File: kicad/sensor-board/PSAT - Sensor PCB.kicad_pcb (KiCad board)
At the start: 2 copper layers, 54.5 x 54.5 mm, 36 parts, among them J1 Conn_01x06, J2 Conn_01x02, J3 Conn_01x03_Pin, J4 Conn_01x03, J6 MCU - Conn_01x04, Q1 Q_NPN_BCE, U1 MPU-6000, U2 BME280, U3 ADXL375, U4 CD-PA1616D, U5 ESP32-CAM

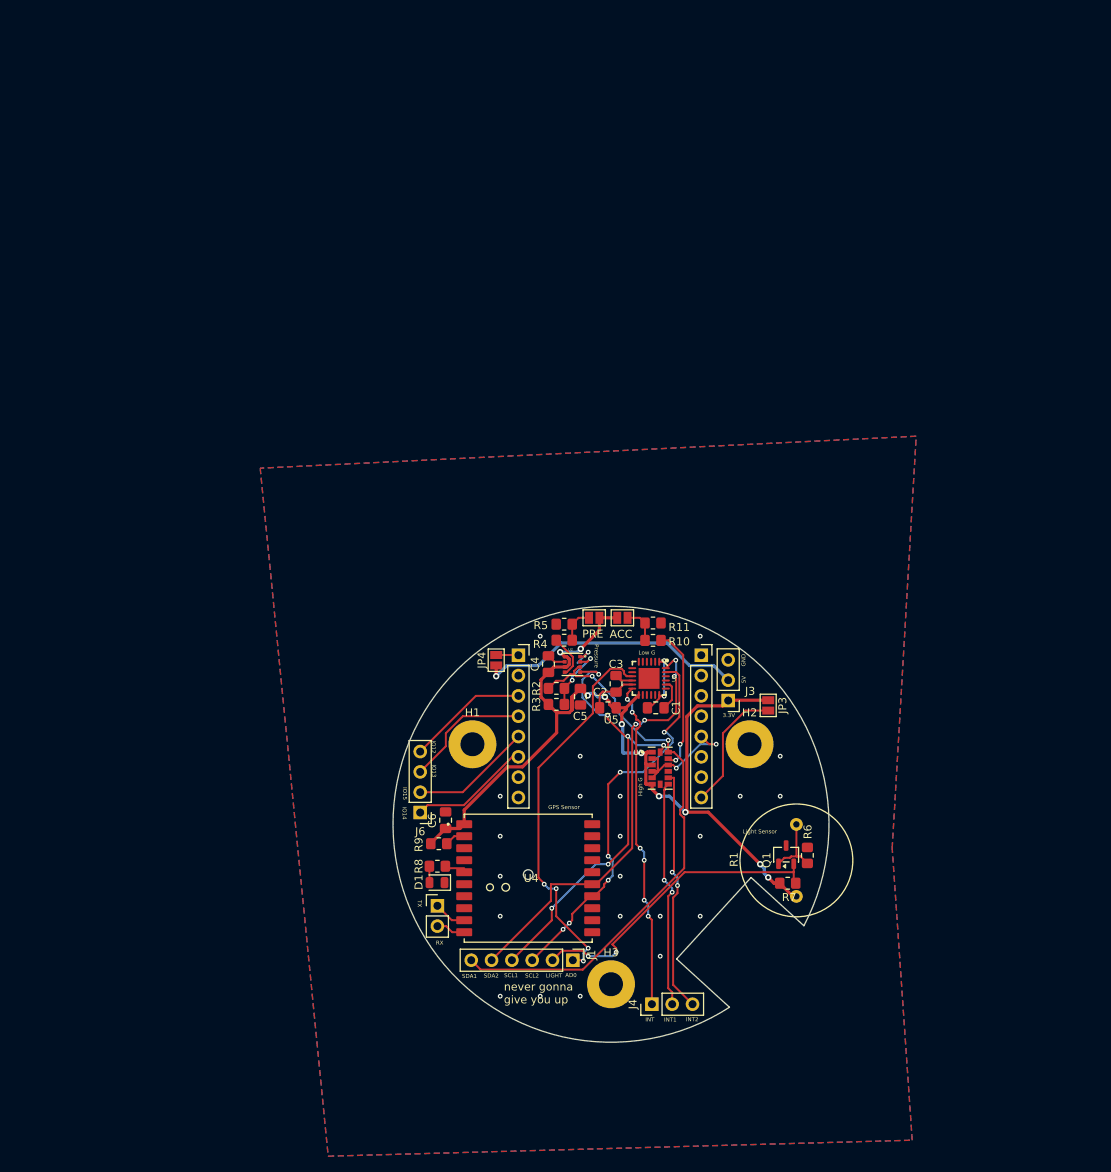
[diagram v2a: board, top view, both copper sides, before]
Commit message: feat: new sensor board pcb & schematic (after feedback)
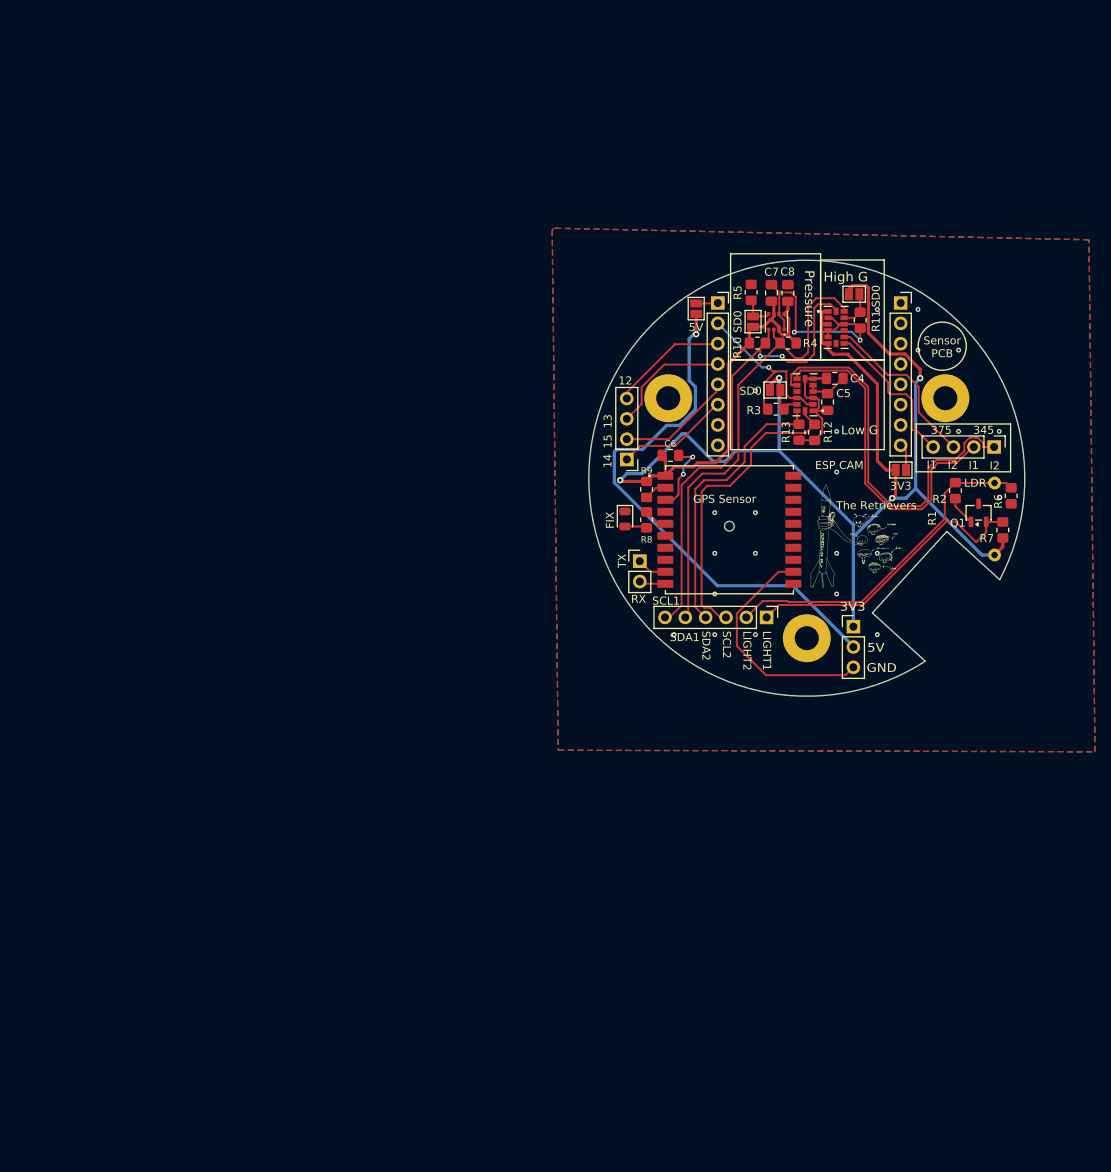
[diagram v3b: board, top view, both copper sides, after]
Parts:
- removed C1: 2.2n, Capacitor_SMD:C_0805_2012Metric_Pad1.18x1.45mm_HandSolder
- removed C2: 0.1n, Capacitor_SMD:C_0805_2012Metric_Pad1.18x1.45mm_HandSolder
- removed C3: 0.1μ, Capacitor_SMD:C_0805_2012Metric_Pad1.18x1.45mm_HandSolder
- removed J4: Conn_01x03, Connector_PinHeader_2.54mm:PinHeader_1x03_P2.54mm_Vertical
- removed JP1, JP2, JP3, JP4: EN_5, Jumper:SolderJumper-2_P1.3mm_Open_Pad1.0x1.5mm
- removed U1: MPU-6000, mpu6000:QFN-24-EP
- added 3V3: EN_5, Jumper:SolderJumper-2_P1.3mm_Open_Pad1.0x1.5mm, F.Cu at (154.1, 96.2)
- added 5V: EN_5, Jumper:SolderJumper-2_P1.3mm_Open_Pad1.0x1.5mm, F.Cu at (128.5, 76.0)
- added C7: 100nF, Capacitor_SMD:C_0805_2012Metric_Pad1.18x1.45mm_HandSolder, F.Cu at (137.9, 74.1)
- added C8: 100nF, Capacitor_SMD:C_0805_2012Metric_Pad1.18x1.45mm_HandSolder, F.Cu at (140.0, 74.1)
- added G***: LOGO, LOGO, F.Cu at (148.5, 105.8)
- added G***: LOGO, LOGO, B.Cu at (142.1, 84.1)
- added J7: Conn_01x06, Connector_PinHeader_2.54mm:PinHeader_1x06_P2.54mm_Vertical, F.Cu at (137.3, 114.7)
- added R12: 4.7k, Resistor_SMD:R_0805_2012Metric_Pad1.20x1.40mm_HandSolder, F.Cu at (143.3, 91.5)
- added R13: 4.7k, Resistor_SMD:R_0805_2012Metric_Pad1.20x1.40mm_HandSolder, F.Cu at (141.3, 91.5)
- added SD0: EN_5, Jumper:SolderJumper-2_P1.3mm_Open_Pad1.0x1.5mm, F.Cu at (138.4, 86.2)
- added SD0: EN_5, Jumper:SolderJumper-2_P1.3mm_Open_Pad1.0x1.5mm, F.Cu at (135.6, 77.7)
- added SD0: EN_5, Jumper:SolderJumper-2_P1.3mm_Open_Pad1.0x1.5mm, F.Cu at (148.2, 74.2)
- added U6: BME280, bme280:PSON65P250X250X100-8N, F.Cu at (138.5, 77.7)
- C4, C5: value 100n -> 100nF
- J1: value Conn_01x06 -> Conn_01x04; footprint Connector_PinHeader_2.54mm:PinHeader_1x06_P2.54mm_Vertical -> Connector_PinHeader_2.54mm:PinHeader_1x04_P2.54mm_Vertical
- Q1: value Q_NPN_BCE -> 2N2222A
- R1: footprint OptoDevice:R_LDR_D13.8mm_P9.0mm_Vertical -> PSAT_Library:ldr
- R10, R4: value 1k5 -> 4.7k
- R2: value 4.7k -> 100k
- R3: value 4.7k -> 1Meg
- R9: value 180k -> 10k
- U2: value BME280 -> ADXL345; footprint bme280:PSON65P250X250X100-8N -> ADXL345:adxl345
- U3: footprint ADXL375:PQFN80P500X300X100-14N -> ADXL375:adxl375
- moved J1 83.0 mm to (165.7, 93.3)
- moved U3 59.3 mm to (146.0, 78.4)
- moved R2 55.7 mm to (160.9, 98.8), turned to -90 degrees
- moved C6 53.6 mm to (125.3, 94.4), turned to 0 degrees
- moved R7 51.7 mm to (166.8, 103.7), turned to -90 degrees
- moved R6 51.7 mm to (167.9, 99.5), turned to 90 degrees
- moved R9 51.3 mm to (122.3, 98.7), turned to -90 degrees
- moved D1 51.2 mm to (119.6, 102.3), turned to -90 degrees
- moved J6 51.1 mm to (119.8, 94.9)
- moved U5 50.6 mm to (142.8, 83.9)
- moved R8 50.6 mm to (122.3, 102.5), turned to -90 degrees
- moved C4 50.6 mm to (145.8, 84.8), turned to 0 degrees
- moved U4 50.3 mm to (132.7, 103.7)
- moved J2 50.0 mm to (121.5, 107.6)
- moved H1 49.7 mm to (125.0, 87.3)
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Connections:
- net /GPS Reset renamed Net-(U4-~{RESET})
- C4 pad 1: 3.3V -> Net-(U2-RESERVED_3)
- C5 pad 1: 3.3V -> Net-(U2-RESERVED_3)
- J1 pad 1: ADO -> INT2_345
- J1 pad 2: LIGHT -> INT1_345
- J1 pad 3: SCL2 -> INT2_375
- J1 pad 4: SCL1 -> INT1_375
- Q1 pad 2: LIGHT -> LIGHT1
- R1 pad 2: Net-(Q1-B) -> LIGHT2
- R10 pad 1: SDO_ACC -> SCL1
- R10 pad 2: Net-(JP2-B) -> 3.3V
- R11 pad 1: Net-(JP2-B) -> GND
- R11 pad 2: GND -> SDO_ACC1
- R2 pad 1: SDA1 -> LIGHT2
- R2 pad 2: Net-(U2-CSB) -> Net-(Q1-B)
- R3 pad 1: 3.3V -> SDO_ACC2
- R3 pad 2: Net-(U2-CSB) -> GND
- R4 pad 1: SDO_PRESSURE -> SDA1
- R4 pad 2: Net-(JP1-B) -> 3.3V
- R5 pad 1: Net-(JP1-B) -> SDO_PRESSURE
- R6 pad 2: Net-(Q1-B) -> LIGHT2
- R7 pad 1: LIGHT -> LIGHT1
- U2 pad 1: GND -> Net-(U2-RESERVED_3)
- U2 pad 2: Net-(U2-CSB) -> GND
- U2 pad 3: SDA1 -> Net-(U2-RESERVED_3)
- U2 pad 4: SCL1 -> GND
- U2 pad 5: SDO_PRESSURE -> GND
- U2 pad 6: 3.3V -> Net-(U2-RESERVED_3)
- U2 pad 7: GND -> Net-(U2-RESERVED_3)
- U2 pad 8: 3.3V -> INT1_345
- U3 pad 12: SDO_ACC -> SDO_ACC1
- U3 pad 8: Net-(J4-Pin_2) -> INT1_375
- U3 pad 9: Net-(J4-Pin_3) -> INT2_375
- U4 pad 14: SCL2 -> unconnected-(U4-RX1/I2C_SCL-Pad14)
- U4 pad 15: SDA2 -> unconnected-(U4-TX1/I2C_SDA-Pad15)
- U5 pad 13: GND -> unconnected-(U5-GND.-Pad13)
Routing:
- net 3.3V: track 125.3 -> 200.8 mm, vias 10 -> 4
- net GND: track 36.6 -> 98.8 mm
- net INT2_345: track 0.00 -> 49.1 mm
- net ADO: track 48.3 -> 0.00 mm, vias 4 -> 0
- net INT1_345: track 0.00 -> 42.5 mm
- net LIGHT2: track 0.00 -> 42.4 mm
- net INT: track 41.6 -> 0.00 mm, vias 6 -> 0
- net LIGHT: track 39.1 -> 0.00 mm, vias 2 -> 0
- net LIGHT1: track 0.00 -> 37.4 mm
- net 5V: track 34.0 -> 67.4 mm
- net Net-(J4-Pin_3): track 30.6 -> 0.00 mm, vias 2 -> 0
- net Net-(J4-Pin_2): track 28.6 -> 0.00 mm, vias 2 -> 0
- net INT2_375: track 0.00 -> 21.2 mm
- net Net-(U2-RESERVED_3): track 0.00 -> 19.8 mm
- net INT1_375: track 0.00 -> 19.4 mm
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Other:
- board text added: "12"
- board text added: "13"
- board text added: "14"
- board text added: "15"
- board text added: "345"
- board text added: "375"
- board text added: "3V3"
- board text added: "ESP CAM"
- board text added: "FIX"
- board text added: "I1"
- board text added: "I2"
- board text added: "LDR"
- board text added: "LIGHT1"
- board text added: "LIGHT2"
- board text added: "Never gonna give you up Never gonna let you down Never gonna run around and desert you Never gonna make you cry Never gonna say goodbye Never gonna tell a lie and hurt you"
- board text added: "Sensor PCB"
- board text added: "The Retrievers"
- board text removed: "3.3V"
- board text removed: "ACC"
- board text removed: "AD0"
- board text removed: "Dear PSAT Team, We couldnt figure out soldermask expansion errors pls help :)"
- board text removed: "INT"
- board text removed: "INT1"
- board text removed: "INT2"
- board text removed: "IO12"
- board text removed: "IO13"
- board text removed: "IO14"
- board text removed: "IO15"
- board text removed: "LIGHT"
- board text removed: "Light Sensor"
- board text removed: "PRE"
- board text removed: "never gonna give you up"

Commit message: feat: Changed labels & started pcb wiring
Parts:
- removed the J1 at (165.7, 93.3)
- removed J7: Conn_01x06, Connector_PinHeader_2.54mm:PinHeader_1x06_P2.54mm_Vertical
- added J4: 5015680407, footprints:CONN_5015680000-SD_04_MOL, F.Cu at (153.7, 104.7)
- added TP1: TestPoint, TestPoint:TestPoint_Pad_D1.0mm, F.Cu at (97.5, 111.0)
- added TP10: TestPoint, TestPoint:TestPoint_Pad_D1.0mm, F.Cu at (101.5, 111.0)
- added TP11: TestPoint, TestPoint:TestPoint_Pad_D1.0mm, F.Cu at (93.4, 111.0)
- added TP12: TestPoint, TestPoint:TestPoint_Pad_D1.0mm, F.Cu at (93.4, 115.0)
- added TP13: TestPoint, TestPoint:TestPoint_Pad_D1.0mm, F.Cu at (97.5, 94.8)
- added TP14: TestPoint, TestPoint:TestPoint_Pad_D1.0mm, F.Cu at (97.5, 98.8)
- added TP2: TestPoint, TestPoint:TestPoint_Pad_D1.0mm, F.Cu at (97.5, 115.0)
- added TP3: TestPoint, TestPoint:TestPoint_Pad_D1.0mm, F.Cu at (93.4, 94.8)
- added TP4: TestPoint, TestPoint:TestPoint_Pad_D1.0mm, F.Cu at (93.4, 98.8)
- added TP5: TestPoint, TestPoint:TestPoint_Pad_D1.0mm, F.Cu at (93.4, 102.9)
- added TP6: TestPoint, TestPoint:TestPoint_Pad_D1.0mm, F.Cu at (93.4, 107.0)
- added TP7: TestPoint, TestPoint:TestPoint_Pad_D1.0mm, F.Cu at (97.5, 102.9)
- added TP8: TestPoint, TestPoint:TestPoint_Pad_D1.0mm, F.Cu at (97.5, 107.0)
- added TP9: TestPoint, TestPoint:TestPoint_Pad_D1.0mm, F.Cu at (101.5, 107.0)
- C5: renamed from C4; value 100nF -> 1uF
- C7: renamed from C5; value 100nF -> 0.1uF
- J2: value Conn_01x02 -> 5015680407; footprint Connector_PinHeader_2.54mm:PinHeader_1x02_P2.54mm_Vertical -> footprints:CONN_5015680000-SD_04_MOL
- J3: value Conn_01x03_Pin -> 5015680407 (X3); footprint Connector_PinHeader_2.54mm:PinHeader_1x03_P2.54mm_Vertical -> footprints:CONN_5015680000-SD_04_MOL
- moved J2 14.5 mm to (132.5, 117.0), turned to 135 degrees
- moved J3 5.32 mm to (148.5, 110.5), turned to 46.5 degrees
- renumbered C8 to C3, C7 to C4, J6 to J1, 5V to JP1, SD0 to JP2, 3V3 to JP3, SD0 to JP4, SD0 to JP5, R11 to R1, R3 to R10, R9 to R11, R4 to R2, R10 to R3, R6 to R4, R1 to R5, R2 to R6, R5 to R7, R7 to R8, R8 to R9, U5 to U1, U6 to U2, U2 to U4, U4 to U5
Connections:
- net SDO_ACC1 renamed HIGH_G_ADDR
- net SDO_ACC2 renamed LOW_G_ADDR
- net SDO_PRESSURE renamed PRESSURE_ADDR
- C3 pad 2: 3.3V -> 3V3_f
- C4 pad 1: 3.3V -> 3V3_f
- C5 pad 1: Net-(U2-RESERVED_3) -> 3V3_f
- C6 pad 1: 3.3V -> 3V3_uf
- C7 pad 1: Net-(U2-RESERVED_3) -> 3V3_f
- J2 pad 1: GPS_UART_TX -> LIGHT2
- J2 pad 2: GPS_UART_RX -> LIGHT1
- J3 pad 1: 3.3V -> GPS_UART_RX
- J3 pad 2: 5V -> GPS_UART_TX
- J3 pad 3: GND -> SDA1
- JP2 pad 1: 3.3V -> 3V3_f
- JP3 pad 1: 3.3V -> 3V3_f
- JP4 pad 1: 3.3V -> 3V3_f
- JP5 pad 1: 3.3V -> 3V3_f
- R11 pad 1: 3.3V -> 3V3_uf
- R12 pad 1: Net-(U2-RESERVED_3) -> 3V3_f
- R13 pad 1: Net-(U2-RESERVED_3) -> 3V3_f
- R2 pad 2: 3.3V -> 3V3_f
- R3 pad 2: 3.3V -> 3V3_f
- R5 pad 1: 3.3V -> 3V3_f
- R8 pad 2: 3.3V -> 3V3_f
- R9 pad 1: Net-(U4-3D-FIX) -> 3V3_f
- U2 pad 2: 3.3V -> 3V3_f
- U2 pad 6: 3.3V -> 3V3_f
- U2 pad 8: 3.3V -> 3V3_f
- U3 pad 1: 3.3V -> 3V3_f
- U3 pad 3: 3.3V -> 3V3_f
- U3 pad 6: 3.3V -> 3V3_f
- U3 pad 7: unconnected-(U3-CS-Pad7) -> 3V3_f
- U4 pad 1: Net-(U2-RESERVED_3) -> 3V3_f
- U4 pad 3: Net-(U2-RESERVED_3) -> 3V3_f
- U4 pad 6: Net-(U2-RESERVED_3) -> 3V3_f
- U4 pad 7: Net-(U2-RESERVED_3) -> 3V3_f
- U5 pad 1: 3.3V -> 3V3_uf
- U5 pad 5: Net-(U4-3D-FIX) -> unconnected-(U5-3D-FIX-Pad5)
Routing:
- net 3.3V: track 200.8 -> 0.00 mm, vias 4 -> 0
- net (no net): track 0.00 -> 200.8 mm, vias 0 -> 4
- net INT2_345: track 49.1 -> 2.18 mm
- net 3V3_f: track 0.00 -> 44.0 mm
- net INT1_345: track 42.5 -> 0.56 mm
- net SCL1: track 61.9 -> 26.3 mm
- net SDA1: track 59.0 -> 25.6 mm
- net LIGHT2: track 42.4 -> 12.3 mm
- net SDA2: track 35.8 -> 5.81 mm
- net SCL2: track 38.9 -> 9.43 mm
- net GND: track 98.8 -> 70.8 mm, vias 27 -> 6
- net LIGHT1: track 37.4 -> 9.95 mm
- net INT2_375: track 21.2 -> 0.71 mm
- net Net-(U2-RESERVED_3): track 19.8 -> 0.00 mm
- net INT1_375: track 19.4 -> 0.98 mm
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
